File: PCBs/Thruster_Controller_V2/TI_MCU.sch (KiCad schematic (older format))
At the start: 16 parts, among them U5 TMS320F28027F

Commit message: More Schematic Updates
- Added initial F280041C symbol, still need to annotate it a bit more
- Created initial BOM estimate
- Still need to complete pinmapping for the MCU
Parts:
- removed U5: TMS320F28027F, Housings_QFP:LQFP-48_7x7mm_Pitch0.5mm, symbol Thruster_Controller:TMS320F28027F
- added U?: TMS320F280041C, Housings_DFN_QFN:QFN-56-1EP_7x7mm_Pitch0.4mm, symbol Thruster_Controller:TMS320F280041C
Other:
- moved on the sheet: C34, C35, C36, C37, C38, D5, L2, L3, R25, R26, R27, R28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

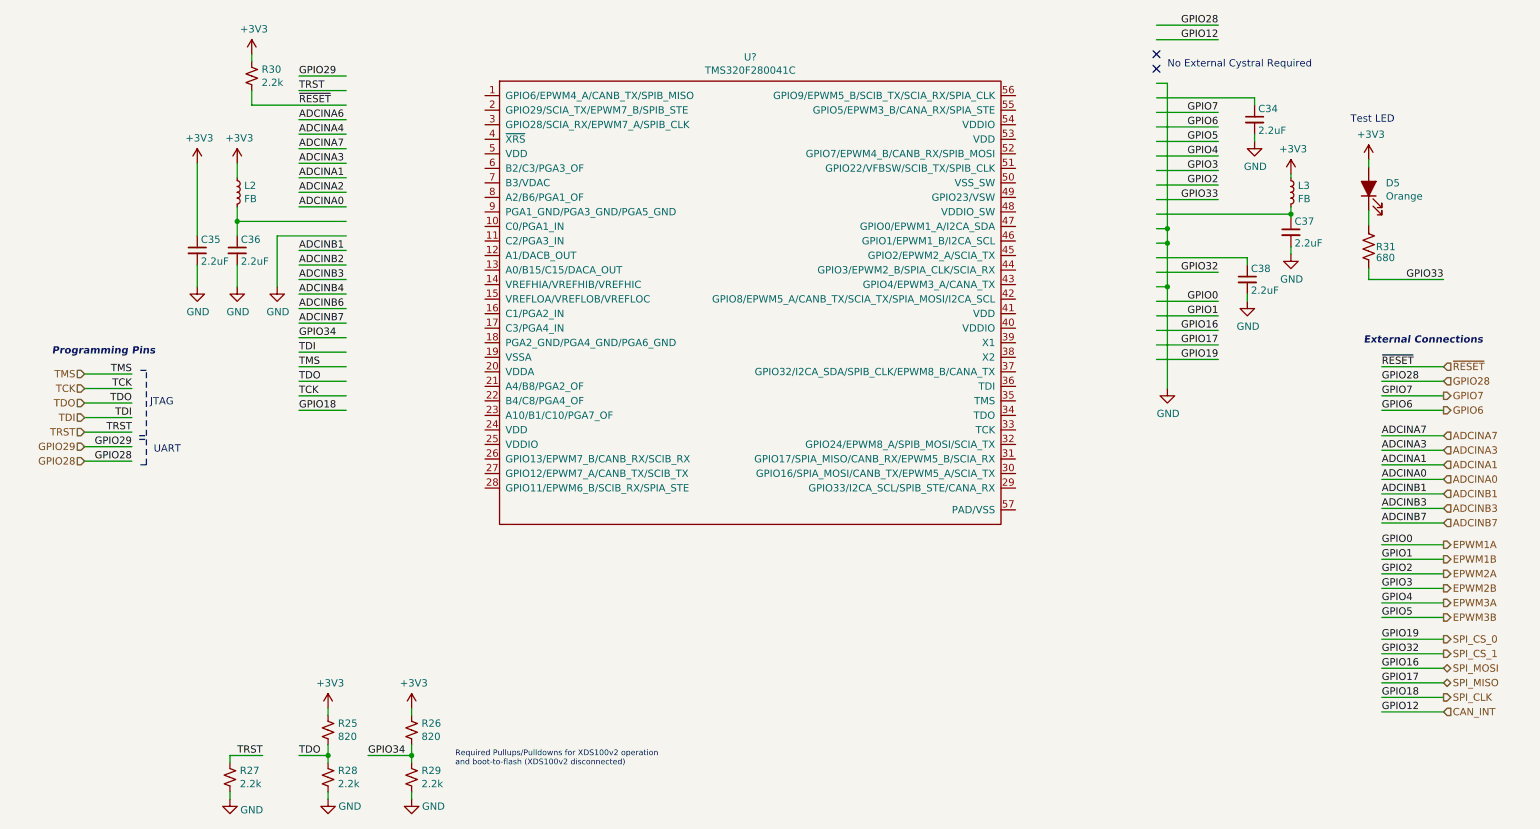
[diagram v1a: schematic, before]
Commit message: Schematic V1
- Completed New Schematic
_ Multiplexed all required signals, may need to redo some arrangments to aid in routing, just because I can and already have to reassign all pins in the SW.
- Created new BOM, only $1 more expensive per board, still might be able to lower that further.
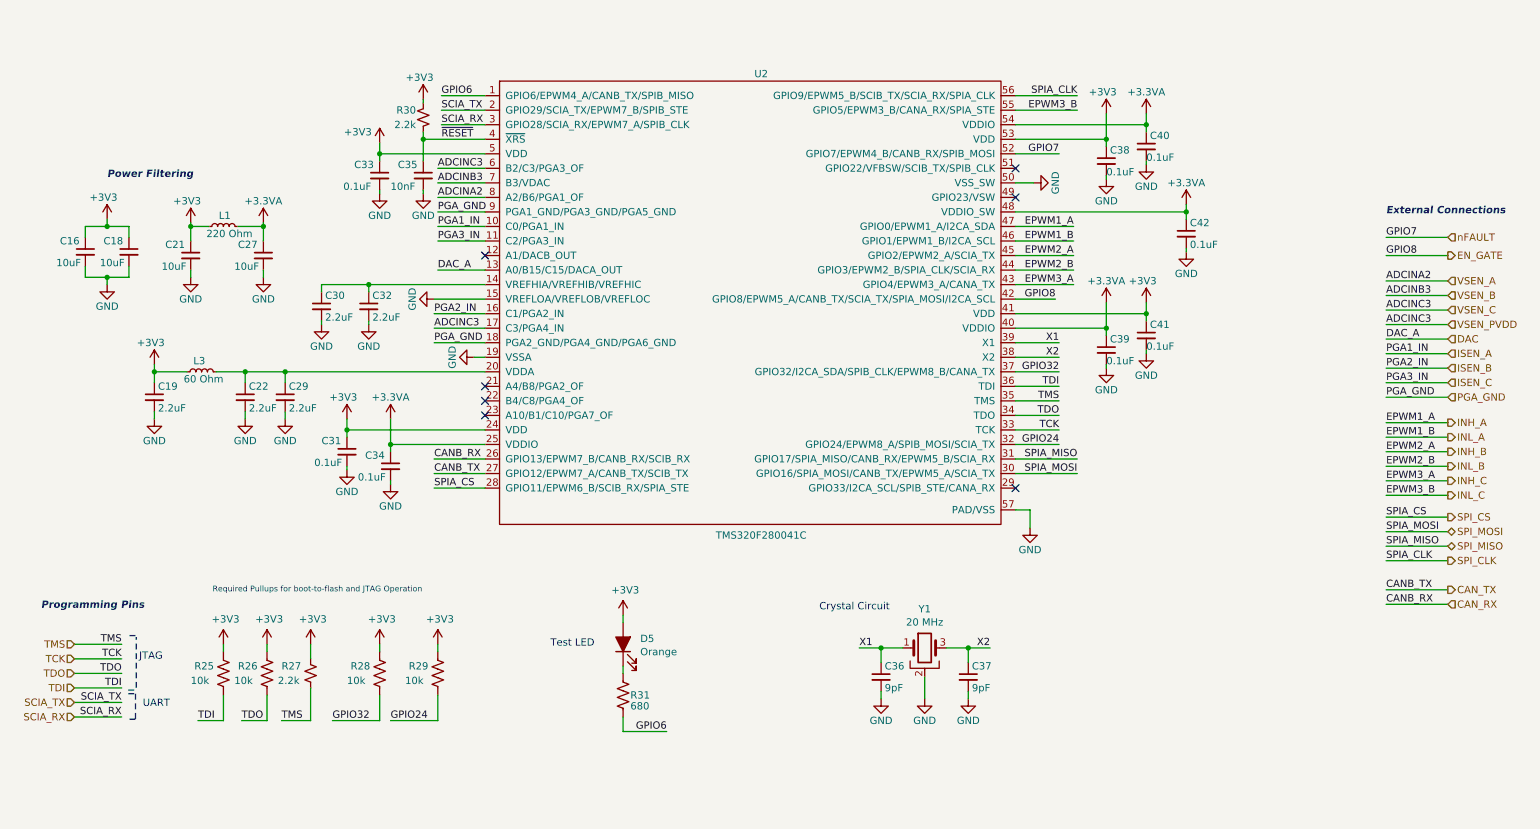
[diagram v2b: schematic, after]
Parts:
- removed L2: FB, Inductors_SMD:L_0805, symbol Device:L_Small
- removed R25, R26: 820, Resistors_SMD:R_0402, symbol Device:R_Small_US
- removed R28, R29: 2.2k, Resistors_SMD:R_0402, symbol Device:R_Small_US
- added C16, C18, C21, C27: 10uF, Capacitors_SMD:C_0603, symbol Device:C_Small
- added C19, C22, C29, C30, C32: 2.2uF, Capacitors_SMD:C_0402, symbol Device:C_Small
- added C31, C33, C39, C40, C41, C42: 0.1uF, Capacitors_SMD:C_0402, symbol Device:C_Small
- added L1: 220 Ohm, Inductors_SMD:L_0402, symbol Device:L_Small
- added R25, R26, R28, R29: 10k, Resistors_SMD:R_0402, symbol Device:R_US
- added Y1: 20 MHz, Crystals:Crystal_SMD_SeikoEpson_FA238-4pin_3.2x2.5mm, symbol Device:Crystal_GND2
- C34, C38: value 2.2uF -> 0.1uF; Digikey 490-10451-1-ND -> 490-10698-1-ND
- C35: value 2.2uF -> 10nF; Digikey 490-10451-1-ND -> 732-7545-1-ND
- C36, C37: value 2.2uF -> 9pF; Digikey 490-10451-1-ND -> 490-5880-1-ND
- L3: value FB -> 60 Ohm
- gave numbers to parts that had none: 1
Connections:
- net labels added: +3.3VA, ADCINC3, CANB_RX, CANB_TX, CAN_RX, CAN_TX, DAC, DAC_A, EN_GATE, EPWM1_A, EPWM1_B, EPWM2_A, EPWM2_B, EPWM3_A, EPWM3_B, GPIO24, GPIO8, INH_A, INH_B, INH_C, INL_A, INL_B, INL_C, ISEN_A, ISEN_B, ISEN_C, PGA1_IN, PGA2_IN, PGA3_IN, PGA_GND, SCIA_RX, SCIA_TX, SPIA_CLK, SPIA_CS, SPIA_MISO, SPIA_MOSI, SPI_CS, VSEN_A, VSEN_B, VSEN_C, VSEN_PVDD, X1, X2, nFAULT
- net labels removed: ADCINA0, ADCINA1, ADCINA3, ADCINA4, ADCINA6, ADCINA7, ADCINB1, ADCINB2, ADCINB4, ADCINB6, ADCINB7, CAN_INT, EPWM1A, EPWM1B, EPWM2A, EPWM2B, EPWM3A, EPWM3B, GPIO0, GPIO1, GPIO12, GPIO16, GPIO17, GPIO18, GPIO19, GPIO2, GPIO28, GPIO29, GPIO3, GPIO33, GPIO34, GPIO4, GPIO5, SPI_CS_0, SPI_CS_1, TRST
- wire segments 114 -> 169
- no-connect marks 2 -> 7
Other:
- note added: "Crystal Circuit"
- note added: "Power Filtering"
- note added: "Required Pullups for boot-to-flash and JTAG Operation"
- note removed: "No External Cystral Required"
- note removed: "Required Pullups/Pulldowns for XDS100v2 operation \nand boot-to-flash (XDS100v2 disconnected)"
- moved on the sheet: D5, L3, R30, R31

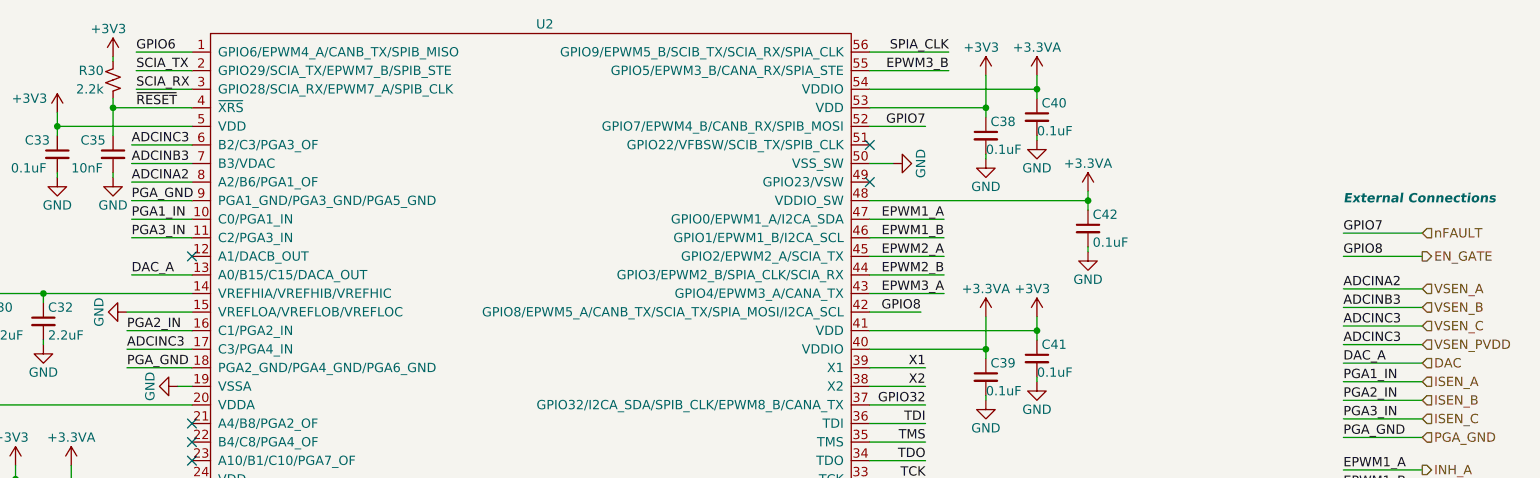
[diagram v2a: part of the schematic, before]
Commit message: Layout Complete
- Initial layout complete
- Most routing complete, still need to clean up everything.
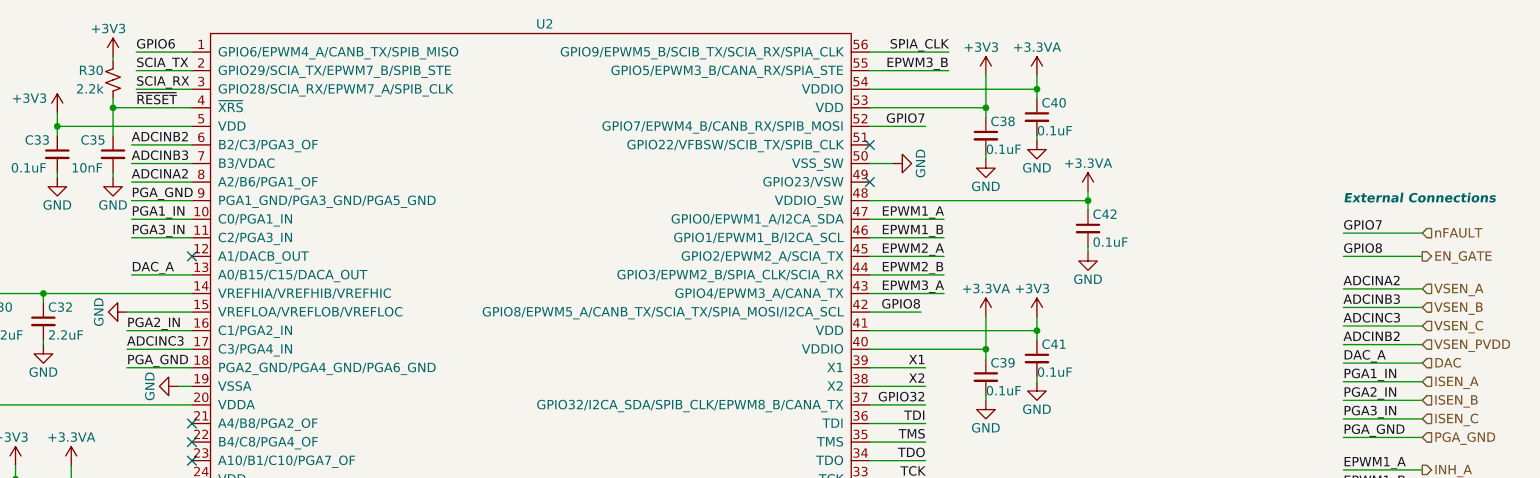
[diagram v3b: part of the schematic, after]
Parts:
- Y1: footprint Crystals:Crystal_SMD_SeikoEpson_FA238-4pin_3.2x2.5mm -> Thruster_Controller:Crystal_SMD_SeikoEpson_FA238-4pin_3.2x2.5mm
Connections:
- net VSEN_C: no longer U2.6 (B2/C3/PGA3_OF)
- new net VSEN_PVDD: U2.6 (B2/C3/PGA3_OF)
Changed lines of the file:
@@
 F 0 "Y1" H 6725 5193 50  0000 C CNN
 F 1 "20 MHz" H 6725 5102 50  0000 C CNN
-F 2 "Crystals:Crystal_SMD_SeikoEpson_FA238-4pin_3.2x2.5mm" H 6725 4925 50  0001 C CNN
+F 2 "Thruster_Controller:Crystal_SMD_SeikoEpson_FA238-4pin_3.2x2.5mm" H 6725 4925 50  0001 C CNN
 F 3 "~" H 6725 4925 50  0001 C CNN
 F 4 "SER3629CT-ND" H 6725 4925 50  0001 C CNN "Digikey"
@@
 	3700 1825 3375 1825
 Text Label 3375 1625 0    50   ~ 0
-ADCINC3
+ADCINB2
 Text Label 3375 1725 0    50   ~ 0
 ADCINB3
@@
 ADCINC3
 Text Label 9900 2700 0    50   ~ 0
-ADCINC3
+ADCINB2
 Text HLabel 10325 2100 2    50   Input ~ 0
 nFAULT

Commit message: Schematic Work / BOM
- Double checking pinout
- Adding digikey PNs for all components, cannot do a mouser run for a small quantity (1-2 boards)
- Generated BOM
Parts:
- U2: Digikey (none) -> 296-F280041CRSHSRCT-ND
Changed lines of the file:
@@
 F 2 "Housings_DFN_QFN:QFN-56-1EP_7x7mm_Pitch0.4mm" H 5600 2825 118 0001 C CNN
 F 3 "http://www.ti.com/lit/ds/symlink/tms320f280041.pdf?ts=1588432897241" H 5600 2925 118 0001 C CNN
-F 4 "" H 5600 2825 50  0001 C CNN "Digikey"
+F 4 "296-F280041CRSHSRCT-ND" H 5600 2825 50  0001 C CNN "Digikey"
 F 5 "595-F280041CRSHSR" H 5600 2825 50  0001 C CNN "Mouser"
 	1    5600 2825

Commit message: VDD fix
- Fixed VDD error, disconnected it from 3V3 rail.
- Will add any more updates to V2.1 after V2 testing
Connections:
- net +3V3: no longer C16.1, C18.1, C31.1, C33.1, C38.1, C41.1, U2.24 (VDD), U2.41 (VDD), U2.5 (VDD), U2.53 (VDD)
- new net: C31.1, U2.24 (VDD)
- new net: C16.1, C41.1, U2.41 (VDD)
- new net: C18.1, C33.1, U2.5 (VDD)
- new net: C38.1, U2.53 (VDD)
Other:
- moved on the sheet: C16, C18
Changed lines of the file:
@@
 	1    0    0    -1
 $EndComp
-Wire Wire Line
-	2975 1525 2975 1450
 $Comp
 L Device:C_Small C33
@@
 Wire Wire Line
 	2975 1575 2975 1525
-Connection ~ 2975 1525
 Wire Wire Line
 	2975 1775 2975 1800
@@
 F 3 "" H 2975 1800 50  0001 C CNN
 	1    2975 1800
-	1    0    0    -1
-$EndComp
-Wire Wire Line
-	2750 3425 2750 3350
-$Comp
-L power:+3V3 #PWR0127
-U 1 1 5F8E04D5
-P 2750 3350
-F 0 "#PWR0127" H 2750 3200 50  0001 C CNN
-F 1 "+3V3" H 2725 3500 50  0000 C CNN
-F 2 "" H 2750 3350 50  0001 C CNN
-F 3 "" H 2750 3350 50  0001 C CNN
-	1    2750 3350
 	1    0    0    -1
 $EndComp
@@
 Wire Wire Line
 	2750 3475 2750 3425
-Connection ~ 2750 3425
 Wire Wire Line
 	2750 3675 2750 3700
@@
 Wire Wire Line
 	7975 1425 7350 1425
-Wire Wire Line
-	7975 1425 7975 1250
-$Comp
-L power:+3V3 #PWR0134
-U 1 1 5F965F87
-P 7975 1250
-F 0 "#PWR0134" H 7975 1100 50  0001 C CNN
-F 1 "+3V3" H 7950 1400 50  0000 C CNN
-F 2 "" H 7975 1250 50  0001 C CNN
-F 3 "" H 7975 1250 50  0001 C CNN
-	1    7975 1250
-	1    0    0    -1
-$EndComp
 $Comp
 L Device:C_Small C38
@@
 Wire Wire Line
 	7975 1475 7975 1425
-Connection ~ 7975 1425
 Wire Wire Line
 	7975 1675 7975 1700
@@
 Wire Wire Line
 	7350 1325 8250 1325
-Wire Wire Line
-	8250 2625 8250 2550
-$Comp
-L power:+3V3 #PWR0142
-U 1 1 5F982626
-P 8250 2550
-F 0 "#PWR0142" H 8250 2400 50  0001 C CNN
-F 1 "+3V3" H 8225 2700 50  0000 C CNN
-F 2 "" H 8250 2550 50  0001 C CNN
-F 3 "" H 8250 2550 50  0001 C CNN
-	1    8250 2550
-	1    0    0    -1
-$EndComp
 $Comp
 L Device:C_Small C41
@@
 Wire Wire Line
 	8250 2675 8250 2625
-Connection ~ 8250 2625
 Wire Wire Line
 	8250 2875 8250 2900
@@
 	-1   0    0    -1
 $EndComp
-$Comp
-L power:+3V3 #PWR0149
-U 1 1 5F8C84EE
-P 2975 1450
-F 0 "#PWR0149" H 2975 1300 50  0001 C CNN
-F 1 "+3V3" H 2825 1525 50  0000 C CNN
-F 2 "" H 2975 1450 50  0001 C CNN
-F 3 "" H 2975 1450 50  0001 C CNN
-	1    2975 1450
-	1    0    0    -1
-$EndComp
 Wire Wire Line
 	3275 1425 3275 1575
@@
 Text Label 7650 2925 2    50   ~ 0
 X2
-Wire Wire Line
-	950  2025 950  2100
-Wire Wire Line
-	1100 2025 950  2025
-Wire Wire Line
-	1100 2025 1100 1975
-Connection ~ 1100 2025
-Wire Wire Line
-	1250 2025 1100 2025
-Wire Wire Line
-	1250 2100 1250 2025
-Wire Wire Line
-	1250 2375 1250 2300
-Wire Wire Line
-	950  2300 950  2375
-Wire Wire Line
-	1100 2375 1250 2375
-Wire Wire Line
-	1100 2375 950  2375
-Connection ~ 1100 2375
-Wire Wire Line
-	1100 2425 1100 2375
 $Comp
 L Device:C_Small C18
 U 1 1 5FA1F497
-P 1250 2200
-F 0 "C18" H 1075 2275 50  0000 L CNN
-F 1 "10uF" H 1050 2125 50  0000 L CNN
-F 2 "Capacitors_SMD:C_0603" H 1250 2200 50  0001 C CNN
-F 3 "~" H 1250 2200 50  0001 C CNN
-F 4 "1276-1119-1-ND" H 1250 2200 50  0001 C CNN "Digikey"
-	1    1250 2200
-	1    0    0    -1
-$EndComp
-$Comp
-L power:GND #PWR0166
-U 1 1 5FA15DFF
-P 1100 2425
-F 0 "#PWR0166" H 1100 2175 50  0001 C CNN
-F 1 "GND" H 1100 2275 50  0000 C CNN
-F 2 "" H 1100 2425 50  0001 C CNN
-F 3 "" H 1100 2425 50  0001 C CNN
-	1    1100 2425
-	1    0    0    -1
-$EndComp
-$Comp
-L power:+3V3 #PWR0167
-U 1 1 5FA07E29
-P 1100 1975
-F 0 "#PWR0167" H 1100 1825 50  0001 C CNN
-F 1 "+3V3" H 1075 2125 50  0000 C CNN
-F 2 "" H 1100 1975 50  0001 C CNN
-F 3 "" H 1100 1975 50  0001 C CNN
-	1    1100 1975
+P 2650 1675
+F 0 "C18" H 2475 1750 50  0000 L CNN
+F 1 "10uF" H 2450 1600 50  0000 L CNN
+F 2 "Capacitors_SMD:C_0603" H 2650 1675 50  0001 C CNN
+F 3 "~" H 2650 1675 50  0001 C CNN
+F 4 "1276-1119-1-ND" H 2650 1675 50  0001 C CNN "Digikey"
+	1    2650 1675
 	1    0    0    -1
 $EndComp
@@
 L Device:C_Small C16
 U 1 1 5F9FF58E
-P 950 2200
-F 0 "C16" H 775 2275 50  0000 L CNN
-F 1 "10uF" H 750 2125 50  0000 L CNN
-F 2 "Capacitors_SMD:C_0603" H 950 2200 50  0001 C CNN
-F 3 "~" H 950 2200 50  0001 C CNN
-F 4 "1276-1119-1-ND" H 950 2200 50  0001 C CNN "Digikey"
-	1    950  2200
+P 8700 2775
+F 0 "C16" H 8525 2850 50  0000 L CNN
+F 1 "10uF" H 8500 2700 50  0000 L CNN
+F 2 "Capacitors_SMD:C_0603" H 8700 2775 50  0001 C CNN
+F 3 "~" H 8700 2775 50  0001 C CNN
+F 4 "1276-1119-1-ND" H 8700 2775 50  0001 C CNN "Digikey"
+	1    8700 2775
 	1    0    0    -1
 $EndComp
@@
 Text Label 9900 2800 0    50   ~ 0
 DAC_A
+Wire Wire Line
+	2650 1575 2650 1525
+Wire Wire Line
+	2650 1525 2975 1525
+Connection ~ 2975 1525
+Wire Wire Line
+	2650 1775 2650 1800
+$Comp
+L power:GND #PWR?
+U 1 1 5F554B55
+P 2650 1800
+F 0 "#PWR?" H 2650 1550 50  0001 C CNN
+F 1 "GND" H 2650 1650 50  0000 C CNN
+F 2 "" H 2650 1800 50  0001 C CNN
+F 3 "" H 2650 1800 50  0001 C CNN
+	1    2650 1800
+	1    0    0    -1
+$EndComp
+Wire Wire Line
+	8250 2625 8700 2625
+Wire Wire Line
+	8700 2625 8700 2675
+Connection ~ 8250 2625
+Wire Wire Line
+	8700 2875 8700 2900
+$Comp
+L power:GND #PWR?
+U 1 1 5F56FB77
+P 8700 2900
+F 0 "#PWR?" H 8700 2650 50  0001 C CNN
+F 1 "GND" H 8700 2750 50  0000 C CNN
+F 2 "" H 8700 2900 50  0001 C CNN
+F 3 "" H 8700 2900 50  0001 C CNN
+	1    8700 2900
+	1    0    0    -1
+$EndComp
 $EndSCHEMATC
